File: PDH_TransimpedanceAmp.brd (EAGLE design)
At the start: 19.1 x 25.4 mm, 21 parts, among them U1 LMH6626, X1 UMC, X2 UMC

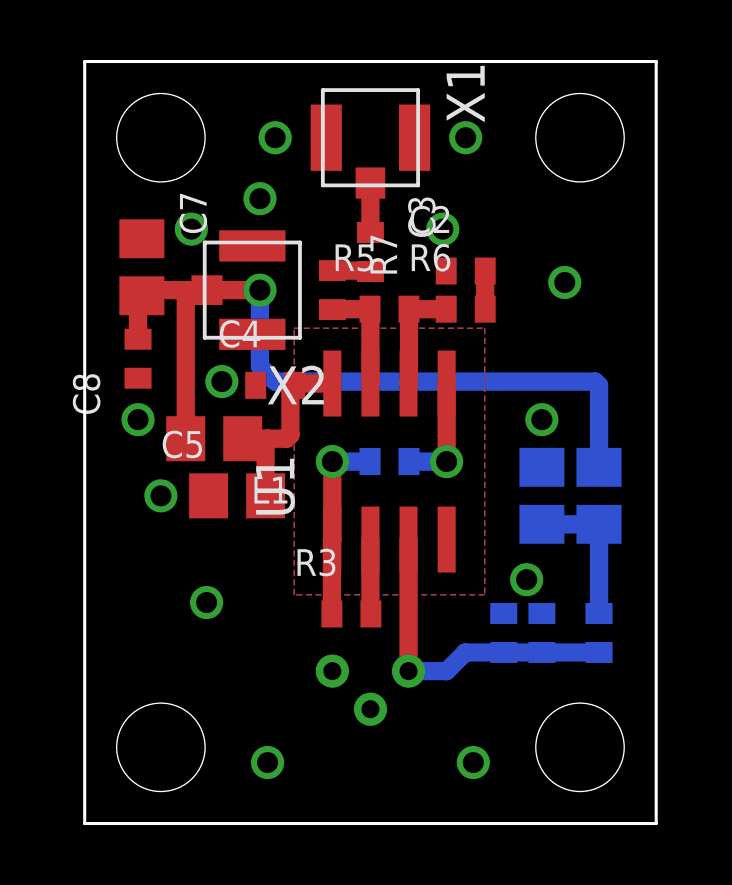
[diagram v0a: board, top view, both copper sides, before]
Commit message: schematic and layout done; a little packed so going to reduce filtering caps
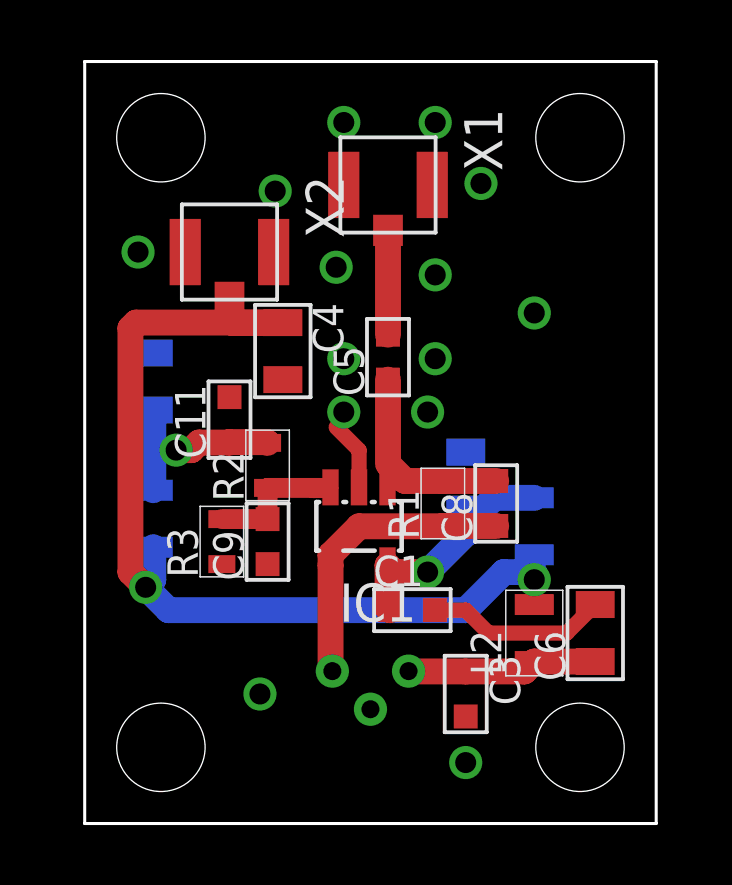
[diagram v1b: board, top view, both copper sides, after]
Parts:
- removed C7: (no value), rlc-jqi:0805
- removed R4, R5, R6, R7: (no value), rlc-jqi:0402
- removed U1: LMH6626, RF_TransimpedanceAmp:SO08
- added C10: 10uF, jqi_passives:C_MLCC_0805
- added C11: 100nF, jqi_passives:C_MLCC_0603
- added C9: (no value), jqi_passives:C_MLCC_0603
- added IC1: LMH6629, opamp-jqi:SOT23-5L
- added L3: (no value), jqi_passives:R_0805
- C1, C3: value (none) -> 100nF; device rlc-jqi:0402 -> jqi_passives:C_MLCC_0603
- C2, C4: value (none) -> 10uF; device rlc-jqi:0402 -> jqi_passives:C_MLCC_0805
- C5: value (none) -> 100nF; device rlc-jqi:0805 -> jqi_passives:C_MLCC_0603
- C6: value (none) -> 10uF; device rlc-jqi:0805 -> jqi_passives:C_MLCC_0805
- C8: device rlc-jqi:0402 -> jqi_passives:C_MLCC_0603
- L1, L2: value Ferrite -> (none); device rlc-jqi:0805 -> jqi_passives:R_0805
- R1: value (none) -> 10k; device rlc-jqi:0402 -> jqi_passives:R_0603
- R2, R3: device rlc-jqi:0402 -> jqi_passives:R_0603
- moved C3 15.1 mm to (12.7, 4.32)
- moved C8 12.9 mm to (13.7, 10.7)
- moved L1 11.1 mm to (15.0, 9.91), flipped to the bottom, turned to 270 degrees
- moved R2 9.66 mm to (6.10, 11.9), flipped to the top, turned to 90 degrees
- moved C2 6.98 mm to (12.7, 11.4), flipped to the bottom, turned to 90 degrees
- moved C5 6.83 mm to (10.1, 15.5), turned to 90 degrees
- moved R1 6.76 mm to (11.9, 10.7), flipped to the top
- moved L2 5.06 mm to (15.0, 6.35), flipped to the top
- moved R3 4.95 mm to (4.57, 9.40), turned to 90 degrees
- moved C6 4.91 mm to (17.0, 6.35), flipped to the top, turned to 90 degrees
- moved C1 4.38 mm to (10.9, 7.11), flipped to the top, turned to 0 degrees
- moved X1 1.68 mm to (10.1, 21.3)
- moved X2 1.48 mm to (4.83, 19.1), turned to 270 degrees
- moved C4 1.17 mm to (6.60, 15.7), turned to 270 degrees
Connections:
- removed net N$5: R3.1, R4.2, U1.1
- removed net N$6: R4.1, U1.5
- removed net N$7: C2.2, R6.2
- removed net N$8: R5.1, R7.2, U1.7
- net GND: now also C1.P$2, C10.P$2, C11.P$2, C2.P$2, C3.P$2, C4.P$2, C6.P$2, C9.P$1, IC1.2, R3.P$1; no longer C1.1, C2.1, C4.1, C5.1, C6.1, C7.1, C8.1, D1.P$3, R2.1, U1.4
- net N$1: now also C8.P$1, D1.P$3, IC1.4, R1.P$1; no longer C1.2, D1.P$1, R1.1, R2.2, U1.3
- net N$10: now also C1.P$1, C2.P$1, IC1.5, L1.P$1; no longer C4.2, C5.2, L1.1, U1.8
- net N$11: now also C5.P$2; no longer C3.1
- net N$2: now also C5.P$1, C8.P$2, IC1.1, R1.P$2; no longer R5.2, R6.1, U1.6
- net N$3: now also C10.P$1, C11.P$1, L3.P$2, R2.P$2; no longer C3.2, R7.1
- net N$4: now also C9.P$2, IC1.3, R2.P$1, R3.P$2; no longer R3.2, U1.2
- net N$9: now also C3.P$1, C6.P$1, D1.P$1, L2.P$1; no longer C6.2, L2.1, R1.2
- net V+: now also C4.P$1, L1.P$2, L2.P$2, L3.P$1; no longer C7.2, C8.2, L1.2, L2.2
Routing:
- net GND: track 0.00 -> 8.37 mm
- net N$5: track 6.35 -> 0.00 mm, vias 1 -> 0
- net V+: track 27.6 -> 33.5 mm, vias 1 -> 2
- net N$3: track 1.28 -> 6.60 mm, vias 0 -> 1
- net N$6: track 3.85 -> 0.00 mm, vias 1 -> 0
- net N$8: track 3.76 -> 0.00 mm
- net N$2: track 3.74 -> 7.41 mm
- net N$4: track 2.49 -> 5.16 mm
- net N$11: track 1.65 -> 3.48 mm
- net N$9: track 4.88 -> 6.37 mm
- net N$10: track 6.60 -> 8.08 mm, vias 0 -> 1
- net N$7: track 1.27 -> 0.00 mm
- net N$1: track 11.0 -> 9.82 mm
- removed copper zone on layer 1, net N$12
- removed copper zone on layer 16, net N$13

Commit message: Printed; prototyped and seems to be working
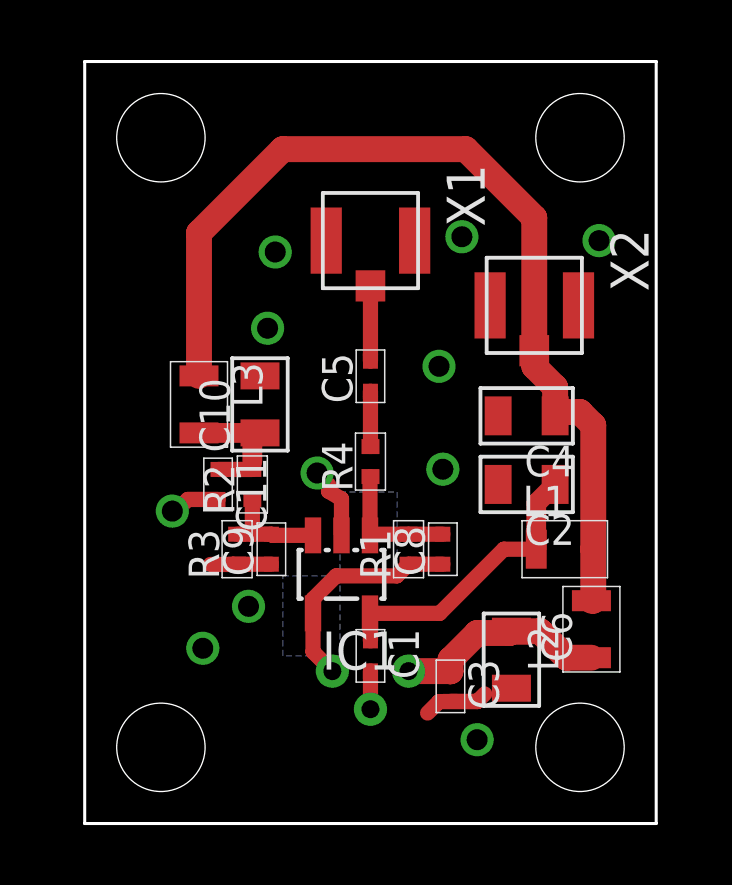
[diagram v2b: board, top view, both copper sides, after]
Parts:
- added R4: 50R, jqi_passives:R_0402
- C1, C11, C3, C5, C8, C9: device jqi_passives:C_MLCC_0603 -> jqi_passives:C_MLCC_0402
- R1, R2, R3: device jqi_passives:R_0603 -> jqi_passives:R_0402
- moved X2 10.3 mm to (15.0, 17.3)
- moved C4 8.41 mm to (14.7, 13.6), turned to 180 degrees
- moved L3 4.10 mm to (3.81, 14.0), flipped to the top, turned to 270 degrees
- moved C10 3.64 mm to (5.84, 14.0), flipped to the top
- moved C6 2.93 mm to (14.2, 5.46), turned to 270 degrees
- moved C8 2.34 mm to (11.9, 9.14)
- moved C11 2.19 mm to (4.45, 11.3), turned to 270 degrees
- moved C1 2.07 mm to (9.53, 5.59), turned to 270 degrees
- moved C2 2.04 mm to (14.7, 11.3), flipped to the top, turned to 180 degrees
- moved X1 1.94 mm to (9.53, 19.4)
- moved L2 1.91 mm to (16.9, 6.48)
- moved R1 1.90 mm to (10.8, 9.14)
- moved IC1 1.70 mm to (8.56, 8.31)
- moved L1 1.27 mm to (16.0, 9.14), flipped to the top, turned to 0 degrees
- moved C5 0.86 mm to (9.53, 14.9)
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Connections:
- new net N$5: C5.P$1, R4.P$2
- net N$2: now also R4.P$1; no longer C5.P$1
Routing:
- net N$2: track 7.41 -> 4.41 mm
- net N$1: track 9.82 -> 7.48 mm
- net N$3: track 6.60 -> 4.50 mm, vias 1 -> 0
- net N$5: track 0.00 -> 1.84 mm
- net N$10: track 8.08 -> 9.77 mm, vias 1 -> 0
- net N$4: track 5.16 -> 3.70 mm
- net GND: track 8.37 -> 9.52 mm, vias 14 -> 11
- net V+: track 33.5 -> 32.4 mm, vias 2 -> 0
- net N$11: track 3.48 -> 2.51 mm
- net N$9: track 6.37 -> 7.25 mm
- added copper zone on layer 16, net N$6
